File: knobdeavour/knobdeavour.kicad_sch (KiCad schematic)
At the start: 97 parts, among them J0 USB_C_Receptacle_USB2.0, J1 BREAKOUT, J2 Conn_01x03_Male, J4 Conn_01x01_Male, K1 KEYSW, K10 KEYSW, K11 KEYSW, K12 KEYSW, K13 KEYSW, K14 KEYSW, K15 KEYSW, K16 KEYSW, K17 KEYSW, K18 KEYSW, K19 KEYSW, K2 KEYSW, K20 KEYSW, K21 KEYSW, K22 KEYSW, K23 KEYSW, K24 KEYSW, K25 KEYSW, K26 KEYSW, K27 KEYSW, K28 KEYSW, K29 KEYSW, K3 KEYSW, K30 KEYSW, K31 KEYSW, K32 KEYSW, K33 KEYSW, K34 KEYSW, K35 KEYSW, K36 KEYSW, K37 KEYSW, K38 KEYSW, K39 KEYSW, K4 KEYSW, K40 KEYSW, K41 KEYSW, K5 KEYSW, K6 KEYSW, K7 KEYSW, K8 KEYSW, K9 KEYSW, SW0 RESET, SW1 RotaryEncoder_Switch, SW2 RotaryEncoder_Switch, U1 NCP1117-3.3_SOT223, U2 W25Q128JVS, U3 RP2040, U44 SRV05-4, Y0 12MHZ Crystal

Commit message: updated schematic, tidying up
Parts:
- removed C10, C8: 1u, Capacitor_SMD:C_0805_2012Metric, symbol Device:C
- removed C11, C12, C13, C14, C6, C7, C9: 100n, Capacitor_SMD:C_0805_2012Metric, symbol Device:C
- removed R3, R4: 27, Resistor_SMD:R_0805_2012Metric, symbol Device:R
- removed U3: RP2040, cipulot_parts:RP2040-QFN-56, symbol MCU_RaspberryPi_RP2040:RP2040
- added C? (x7): 100n, Capacitor_SMD:C_0805_2012Metric, symbol Device:C
- added C? (x2): 1u, Capacitor_SMD:C_0805_2012Metric, symbol Device:C
- added R8: 10K, Resistor_SMD:R_0805_2012Metric, symbol Device:R
- added R? (x2): 27, Resistor_SMD:R_0805_2012Metric, symbol Device:R
- added SW2: SW_PUSH, Keebio-Parts:SW_SPST_TL3342, symbol cipulot_parts:SW_PUSH
- added U?: RP2040, cipulot_parts:RP2040-QFN-56, symbol MCU_RaspberryPi_RP2040:RP2040
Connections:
- net +1V1: now also C?.1, C?.1, C?.1, U?.23 (DVDD), U?.45 (VREG_VOUT), U?.50 (DVDD)
- net +3V3: now also C?.1, C?.1, C?.1, C?.1, C?.1, C?.1, R8.2, U?.1 (IOVDD), U?.10 (IOVDD), U?.22 (IOVDD), U?.33 (IOVDD), U?.42 (IOVDD), U?.43 (ADC_AVDD), U?.44 (VREG_IN), U?.48 (USB_VDD), U?.49 (IOVDD)
- net COL0: now also U?.9 (GPIO7)
- net COL1: now also U?.11 (GPIO8)
- net COL10: now also U?.32 (GPIO21)
- net COL2: now also U?.12 (GPIO9)
- net COL3: now also U?.14 (GPIO11)
- net COL4: now also U?.13 (GPIO10)
- net COL5: now also U?.2 (GPIO0)
- net COL6: now also U?.28 (GPIO17)
- net COL7: now also U?.29 (GPIO18)
- net COL8: now also U?.30 (GPIO19)
- net COL9: now also U?.31 (GPIO20)
- net GND: now also C?.2, C?.2, C?.2, C?.2, C?.2, C?.2, C?.2, C?.2, C?.2, SW2.1, U?.19 (TESTEN), U?.57 (GND)
- net GPIO26_ADC0: now also U?.38 (GPIO26_ADC0)
- net GPIO27_ADC1: now also U?.39 (GPIO27_ADC1)
- net GPIO28_ADC2: now also U?.40 (GPIO28_ADC2)
- net GPIO29_ADC3: now also U?.41 (GPIO29_ADC3)
- net KNOB2_L: now also U?.7 (GPIO5)
- net KNOB2_R: now also U?.6 (GPIO4)
- net KNOB_COL: now also U?.27 (GPIO16)
- net KNOB_L: now also U?.35 (GPIO23)
- net KNOB_R: now also U?.34 (GPIO22)
- net LED_GLOW: now also U?.15 (GPIO12)
- net QSPI_SCLK: now also U?.52 (QSPI_SCLK)
- net QSPI_SD0: now also U?.53 (QSPI_SD0)
- net QSPI_SD1: now also U?.55 (QSPI_SD1)
- net QSPI_SD2: now also U?.54 (QSPI_SD2)
- net QSPI_SD3: now also U?.51 (QSPI_SD3)
- net QSPI_SS: now also U?.56 (QSPI_SS)
- net ROW0: now also U?.8 (GPIO6)
- net ROW1: now also U?.16 (GPIO13)
- net ROW2: now also U?.17 (GPIO14)
- net ROW3: now also U?.18 (GPIO15)
- net RUN: now also R8.1, SW2.2, U?.26 (RUN)
- net SWCLK: now also U?.24 (SWCLK)
- net SWD: now also U?.25 (SWD)
- net USB_D+: now also R?.1
- net USB_D-: now also R?.1
- net XIN: now also U?.20 (XIN)
- net XOUT: now also U?.21 (XOUT)
- new net: R?.2, U?.46 (USB_DM)
- new net: R?.2, U?.47 (USB_DP)
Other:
- note added: "Breakout"
- note added: "Crystal"
- note added: "Encoder"
- note added: "Flash memory"
- note added: "Keyboard-matrice"
- note added: "LDO 5V -> 3.3V"
- note added: "MCU"
- note added: "USB ESD-Protection"
- note removed: "Flash"
- moved on the sheet: C1, C17, C2, C3, C4, C5, D1, D10, D11, D12, D13, D14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

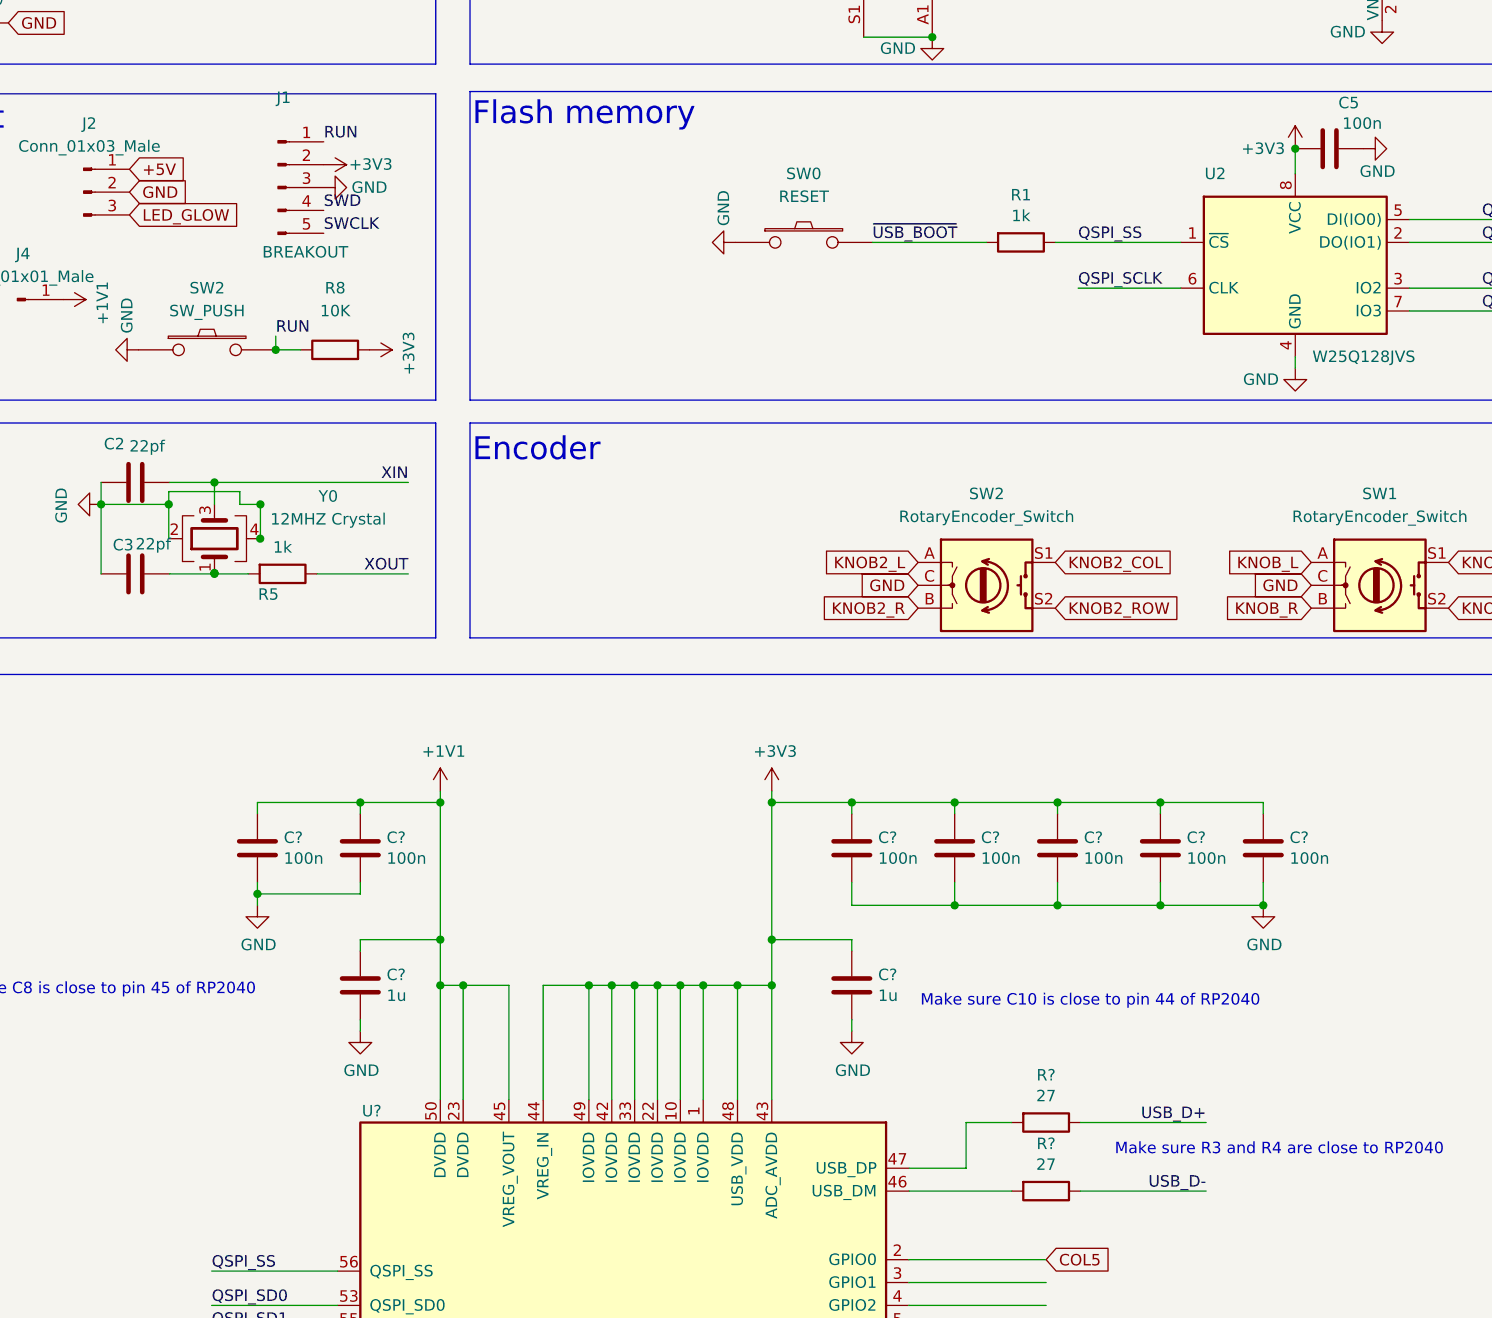
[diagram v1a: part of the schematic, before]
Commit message: updated pcb, added second btn
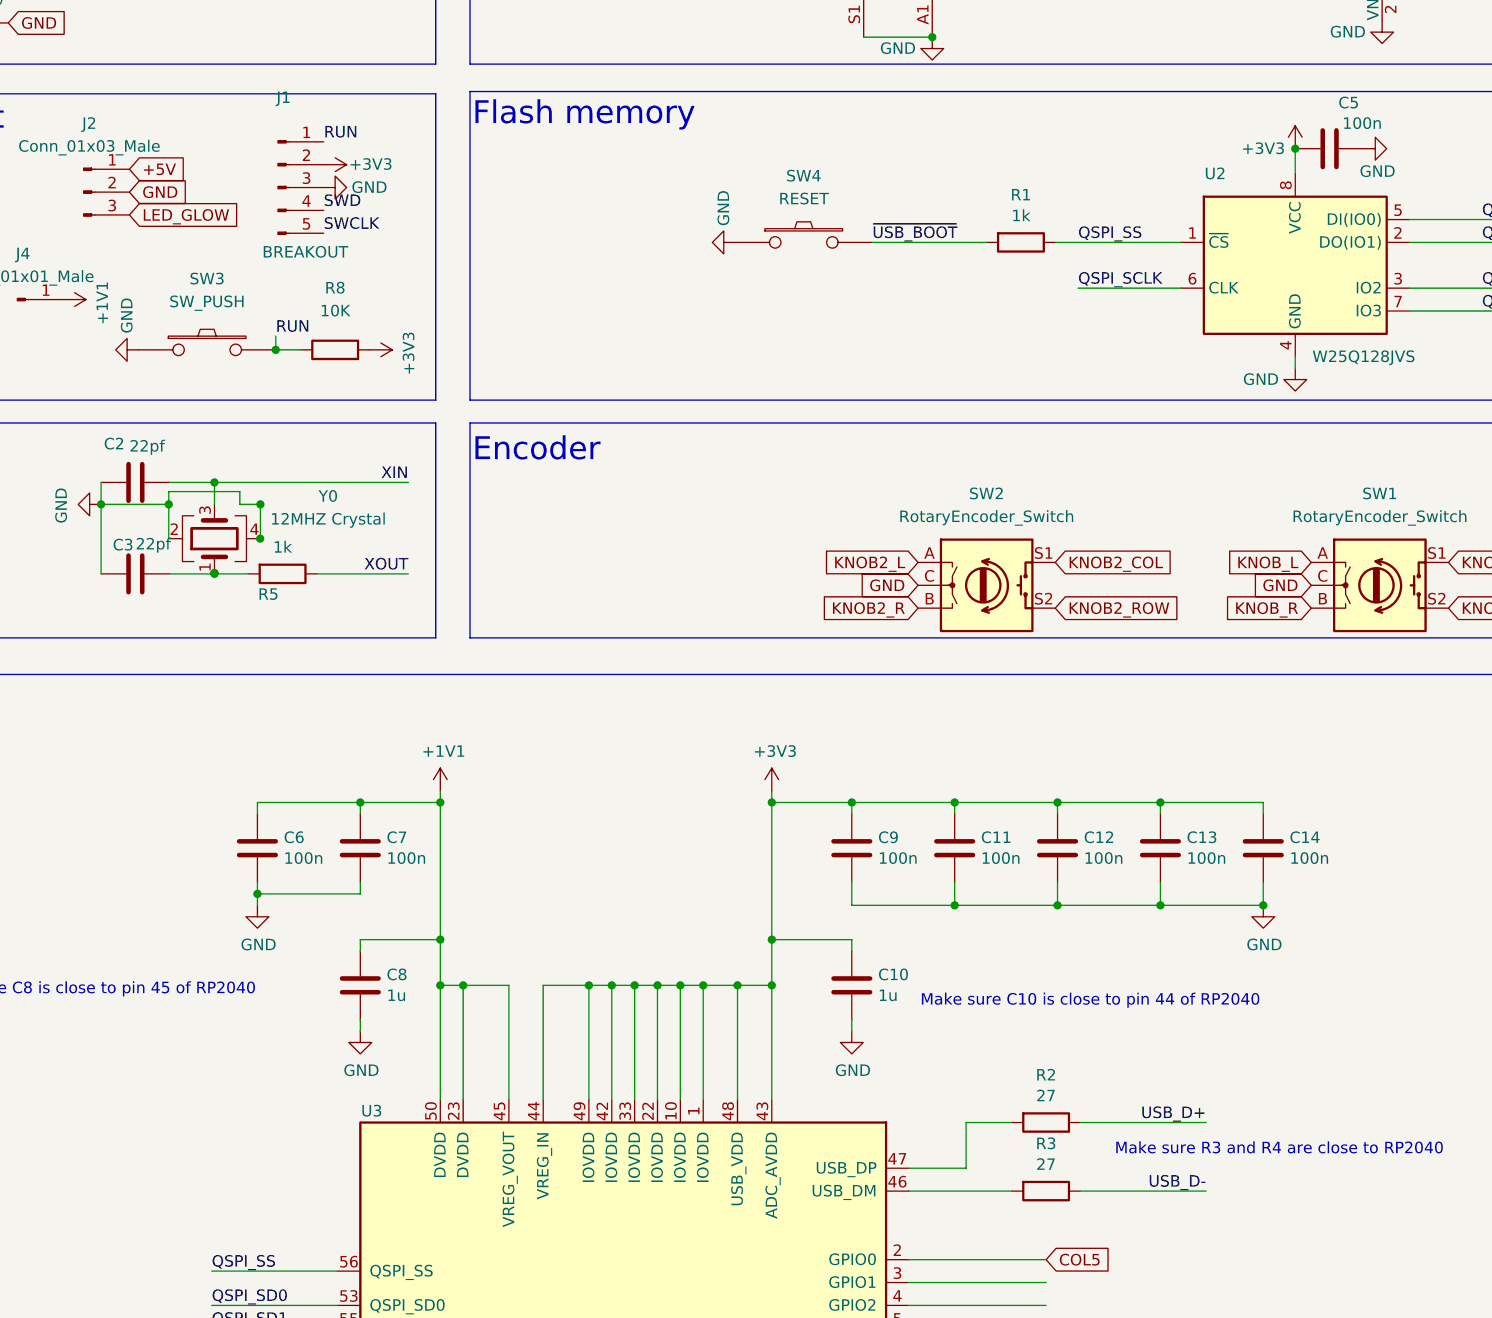
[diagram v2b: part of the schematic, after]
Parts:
- gave numbers to parts that had none: 12
- renumbered SW2 to SW3, SW0 to SW4

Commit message: updated case and images
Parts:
- D1, D10, D11, D12, D13, D14, D15, D16, D17, D18, D19, D2, D20, D21, D22, D3, D4, D5, D6, D7, D8, D9: LCSC (none) -> C68978
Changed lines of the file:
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@@
+      (effects (font (size 1.27 1.27)) hide)
+    )
+    (property "LCSC" "C68978" (id 4) (at 416.052 342.646 0)
       (effects (font (size 1.27 1.27)) hide)
     )
@@
       (effects (font (size 1.27 1.27)) hide)
     )
+    (property "LCSC" "C68978" (id 4) (at 315.976 329.184 0)
+      (effects (font (size 1.27 1.27)) hide)
+    )
     (pin "1")
     (pin "2")
@@
       (effects (font (size 1.27 1.27)) hide)
     )
+    (property "LCSC" "C68978" (id 4) (at 367.792 342.9 0)
+      (effects (font (size 1.27 1.27)) hide)
+    )
     (pin "1")
     (pin "2")
@@
       (effects (font (size 1.27 1.27)) hide)
     )
+    (property "LCSC" "C68978" (id 4) (at 315.976 359.664 0)
+      (effects (font (size 1.27 1.27)) hide)
+    )
     (pin "1")
     (pin "2")
@@
     )
     (property "Datasheet" "https://assets.nexperia.com/documents/data-sheet/BAV70_SER.pdf" (id 3) (at 416.052 328.676 0)
+      (effects (font (size 1.27 1.27)) hide)
+    )
+    (property "LCSC" "C68978" (id 4) (at 416.052 328.676 0)
       (effects (font (size 1.27 1.27)) hide)
     )
@@
     )
     (property "Datasheet" "https://assets.nexperia.com/documents/data-sheet/BAV70_SER.pdf" (id 3) (at 464.058 311.912 0)
+      (effects (font (size 1.27 1.27)) hide)
+    )
+    (property "LCSC" "C68978" (id 4) (at 464.058 311.912 0)
       (effects (font (size 1.27 1.27)) hide)
     )
@@
       (effects (font (size 1.27 1.27)) hide)
     )
+    (property "LCSC" "C68978" (id 4) (at 266.7 329.438 0)
+      (effects (font (size 1.27 1.27)) hide)
+    )
     (pin "1")
     (pin "2")
@@
       (effects (font (size 1.27 1.27)) hide)
     )
+    (property "LCSC" "C68978" (id 4) (at 266.7 312.928 0)
+      (effects (font (size 1.27 1.27)) hide)
+    )
     (pin "1")
     (pin "2")
@@
     )
     (property "Datasheet" "https://assets.nexperia.com/documents/data-sheet/BAV70_SER.pdf" (id 3) (at 464.058 358.902 0)
+      (effects (font (size 1.27 1.27)) hide)
+    )
+    (property "LCSC" "C68978" (id 4) (at 464.058 358.902 0)
       (effects (font (size 1.27 1.27)) hide)
     )
@@
       (effects (font (size 1.27 1.27)) hide)
     )
+    (property "LCSC" "C68978" (id 4) (at 315.976 343.154 0)
+      (effects (font (size 1.27 1.27)) hide)
+    )
     (pin "1")
     (pin "2")
@@
       (effects (font (size 1.27 1.27)) hide)
     )
+    (property "LCSC" "C68978" (id 4) (at 464.058 342.392 0)
+      (effects (font (size 1.27 1.27)) hide)
+    )
     (pin "1")
     (pin "2")
@@
       (effects (font (size 1.27 1.27)) hide)
     )
+    (property "LCSC" "C68978" (id 4) (at 496.316 328.676 0)
+      (effects (font (size 1.27 1.27)) hide)
+    )
     (pin "1")
     (pin "2")
@@
       (effects (font (size 1.27 1.27)) hide)
     )
+    (property "LCSC" "C68978" (id 4) (at 496.316 342.646 0)
+      (effects (font (size 1.27 1.27)) hide)
+    )
     (pin "1")
     (pin "2")
@@
       (effects (font (size 1.27 1.27)) hide)
     )
+    (property "LCSC" "C68978" (id 4) (at 496.316 312.166 0)
+      (effects (font (size 1.27 1.27)) hide)
+    )
     (pin "1")
     (pin "2")
@@
       (effects (font (size 1.27 1.27)) hide)
     )
+    (property "LCSC" "C68978" (id 4) (at 416.052 359.156 0)
+      (effects (font (size 1.27 1.27)) hide)
+    )
     (pin "1")
     (pin "2")
@@
     )
     (property "Datasheet" "https://assets.nexperia.com/documents/data-sheet/BAV70_SER.pdf" (id 3) (at 464.058 328.422 0)
+      (effects (font (size 1.27 1.27)) hide)
+    )
+    (property "LCSC" "C68978" (id 4) (at 464.058 328.422 0)
       (effects (font (size 1.27 1.27)) hide)
     )
@@
       (effects (font (size 1.27 1.27)) hide)
     )
+    (property "LCSC" "C68978" (id 4) (at 266.7 359.918 0)
+      (effects (font (size 1.27 1.27)) hide)
+    )
     (pin "1")
     (pin "2")
@@
       (effects (font (size 1.27 1.27)) hide)
     )
+    (property "LCSC" "C68978" (id 4) (at 315.976 312.674 0)
+      (effects (font (size 1.27 1.27)) hide)
+    )
     (pin "1")
     (pin "2")
@@
       (effects (font (size 1.27 1.27)) hide)
     )
+    (property "LCSC" "C68978" (id 4) (at 367.792 328.93 0)
+      (effects (font (size 1.27 1.27)) hide)
+    )
     (pin "1")
     (pin "2")
@@
       (effects (font (size 1.27 1.27)) hide)
     )
+    (property "LCSC" "C68978" (id 4) (at 367.792 312.42 0)
+      (effects (font (size 1.27 1.27)) hide)
+    )
     (pin "1")
     (pin "2")
@@
       (effects (font (size 1.27 1.27)) hide)
     )
+    (property "LCSC" "C68978" (id 4) (at 266.7 343.408 0)
+      (effects (font (size 1.27 1.27)) hide)
+    )
     (pin "1")
     (pin "2")
@@
       (effects (font (size 1.27 1.27)) hide)
     )
+    (property "LCSC" "C68978" (id 4) (at 416.052 312.166 0)
+      (effects (font (size 1.27 1.27)) hide)
+    )
